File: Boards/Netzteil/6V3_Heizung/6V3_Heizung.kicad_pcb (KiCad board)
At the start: 2 copper layers, 100 x 80 mm, 65 parts, among them P1 7V5_AC, P2 12V_DC, P3 6V3_DC_1, P4 6V3_DC_2, P5 Relais, Q1 IRF540N, Q2 IRF540N, Q3 BS170, U1 TL072, U2 LM393

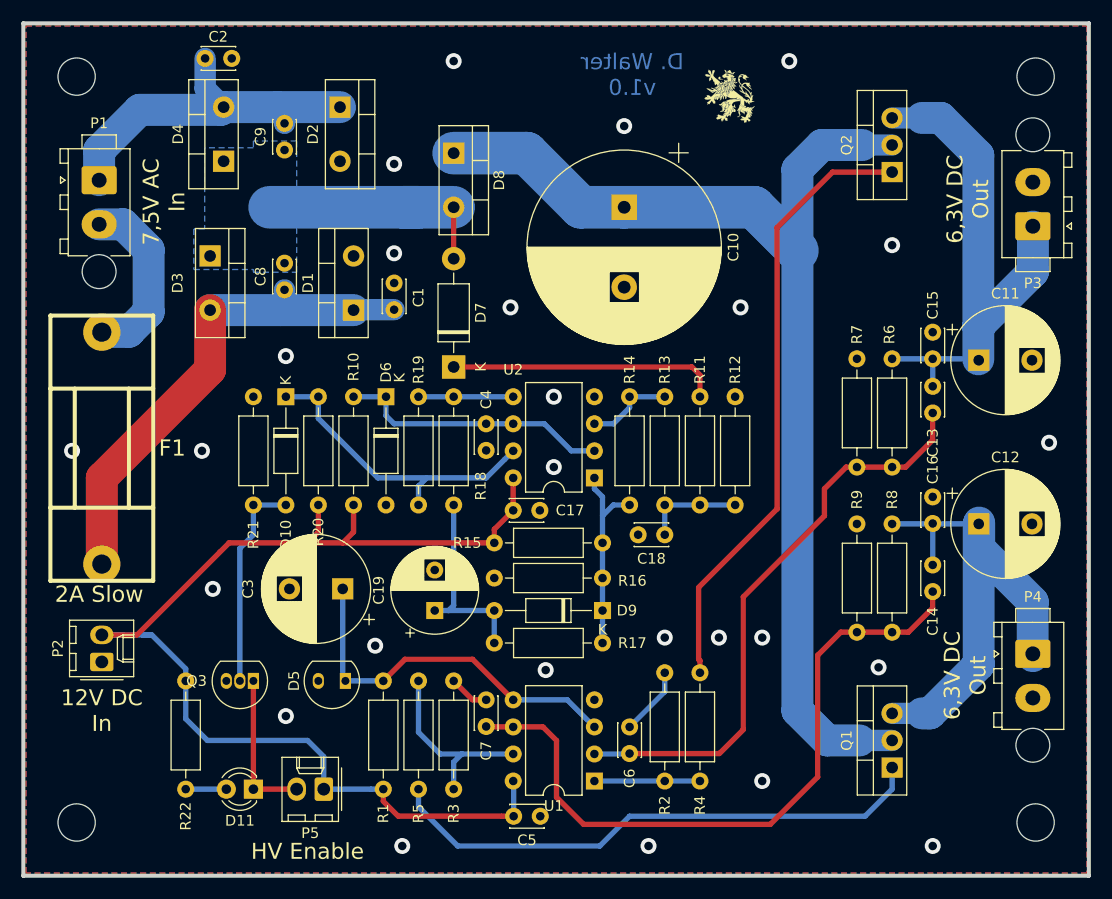
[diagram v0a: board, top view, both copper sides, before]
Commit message: Added Power LEDs
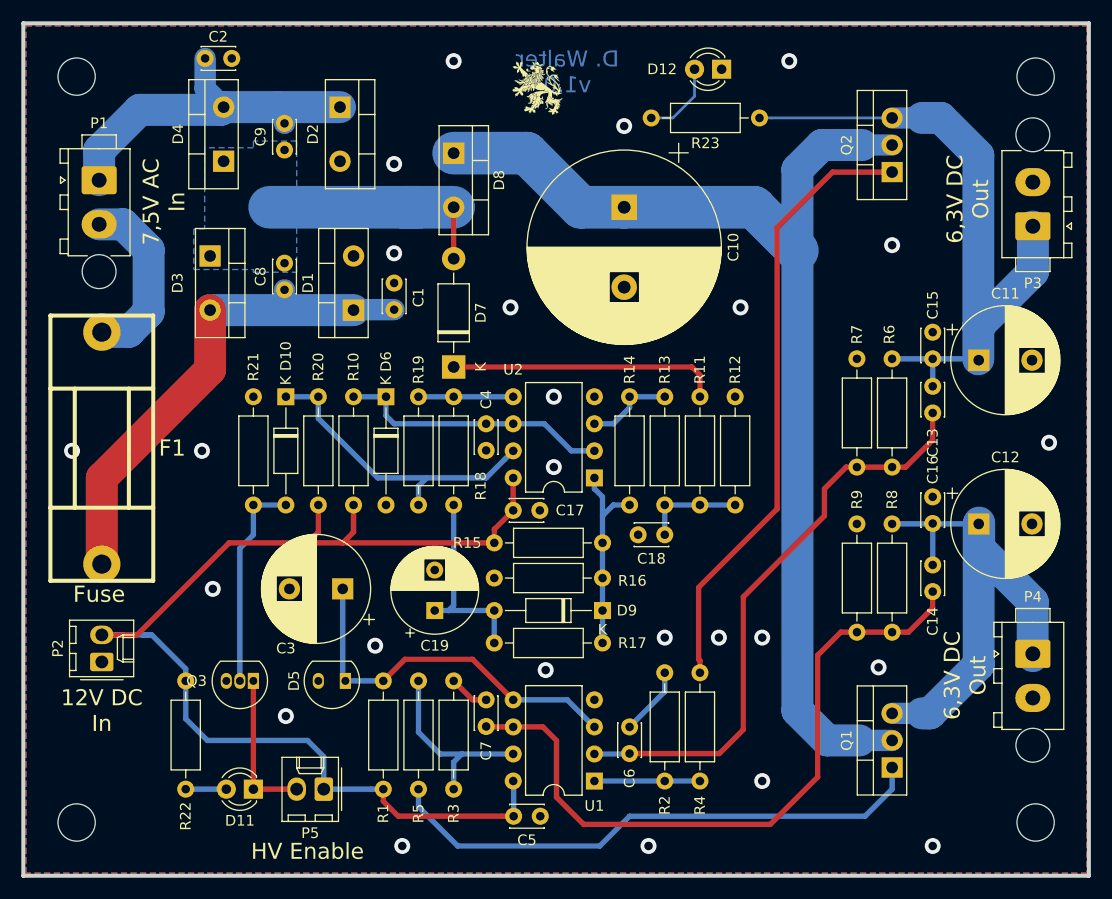
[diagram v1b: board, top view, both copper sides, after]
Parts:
- added D12: LED, LED_THT:LED_D3.0mm, F.Cu at (125.1, 43.2)
- added R23: 23k, Resistor_THT:R_Axial_DIN0207_L6.3mm_D2.5mm_P10.16mm_Horizontal, F.Cu at (128.7, 47.8)
- F1: value 2A Slow -> Fuse
- moved G*** 18.1 mm to (107.8, 45.0)
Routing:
- net Net-(C11-Pad1): track 52.8 -> 65.3 mm
- net Net-(D12-Pad2): track 0.00 -> 7.45 mm
- net GND: vias 26 -> 25

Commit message: Adjusted Silkscreen
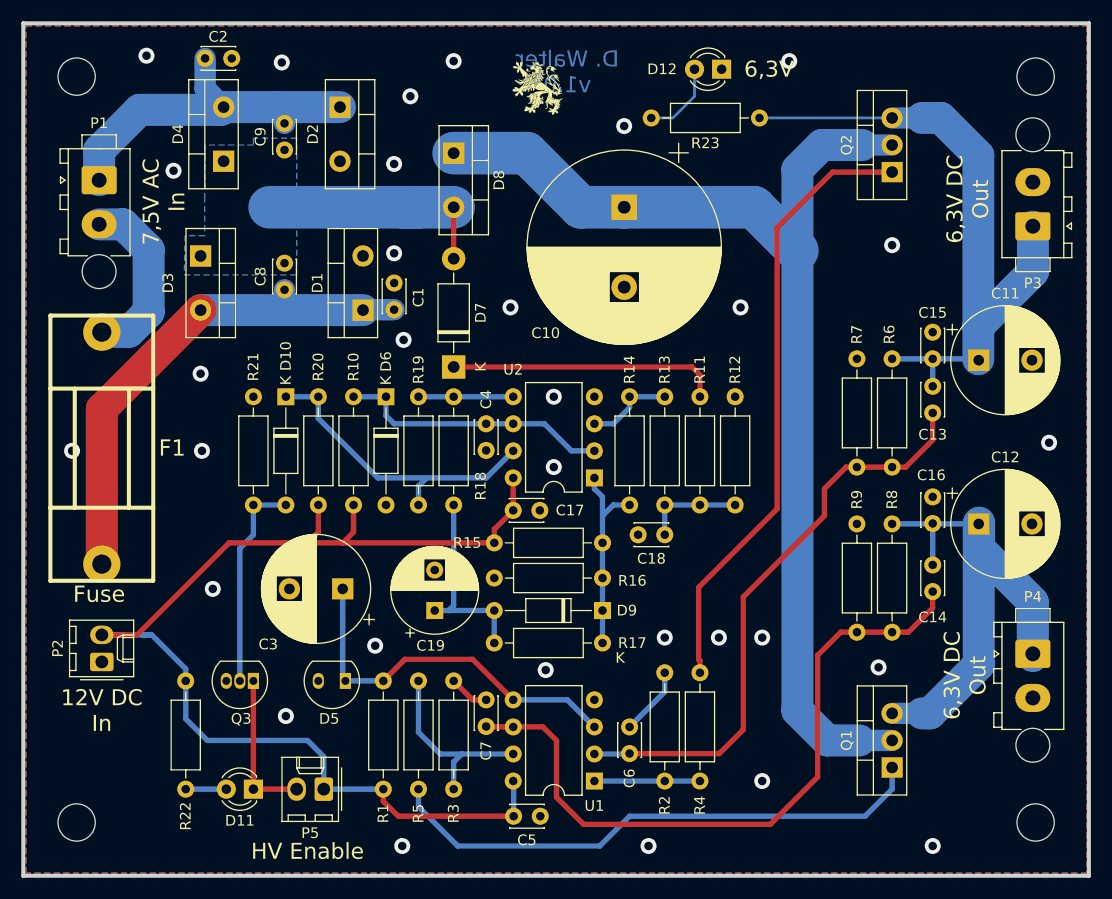
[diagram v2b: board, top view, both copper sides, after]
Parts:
- moved D1 0.89 mm to (91.4, 65.8)
- moved D3 0.89 mm to (76.2, 60.7)
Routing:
- net Net-(C1-Pad1): track 47.4 -> 48.8 mm
- net GND: vias 25 -> 31
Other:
- board text added: "6,3V"
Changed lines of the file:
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@@
   (general
     (thickness 1.6)
-    (drawings 6)
-    (tracks 240)
+    (drawings 7)
+    (tracks 244)
     (zones 0)
     (modules 67)
@@
     (47 F.CrtYd user)
     (48 B.Fab user)
-    (49 F.Fab user)
+    (49 F.Fab user hide)
   )
   (setup
-    (last_trace_width 0.25)
+    (last_trace_width 3)
     (user_trace_width 0.5)
     (user_trace_width 1)
@@
       (effects (font (size 1 1) (thickness 0.15)))
     )
-    (fp_text user K (at 0 -1.8) (layer F.SilkS)
+    (fp_text user K (at -1.651 -4.445) (layer F.SilkS)
       (effects (font (size 1 1) (thickness 0.15)))
     )
@@
     (descr "TO-92 leads in-line, narrow, oval pads, drill 0.75mm (see NXP sot054_po.pdf)")
     (tags "to-92 sc-43 sc-43a sot54 PA33 transistor")
-    (fp_text reference Q3 (at 5.334 0) (layer F.SilkS)
+    (fp_text reference Q3 (at 1.143 -3.556) (layer F.SilkS)
       (effects (font (size 1 1) (thickness 0.15)))
     )
@@
     (descr "CP, Radial series, Radial, pin pitch=3.80mm, , diameter=8mm, Electrolytic Capacitor")
     (tags "CP Radial series Radial pin pitch 3.80mm  diameter 8mm Electrolytic Capacitor")
-    (fp_text reference C19 (at -3.302 0 180) (layer F.SilkS)
+    (fp_text reference C19 (at -3.302 -0.381 180) (layer F.SilkS)
       (effects (font (size 1 1) (thickness 0.15)))
     )
@@
     (descr "CP, Radial series, Radial, pin pitch=7.50mm, , diameter=18mm, Electrolytic Capacitor")
     (tags "CP Radial series Radial pin pitch 7.50mm  diameter 18mm Electrolytic Capacitor")
-    (fp_text reference C10 (at 3.75 -10.25 270) (layer F.SilkS)
+    (fp_text reference C10 (at 11.811 7.366) (layer F.SilkS)
       (effects (font (size 1 1) (thickness 0.15)))
     )
@@
     (descr "TO-92 2-pin leads in-line, narrow, oval pads, drill 0.75mm (see NXP sot054_po.pdf)")
     (tags "to-92 sc-43 sc-43a sot54 PA33 diode SOD70")
-    (fp_text reference D5 (at 4.826 0 270) (layer F.SilkS)
+    (fp_text reference D5 (at 1.524 -3.556) (layer F.SilkS)
       (effects (font (size 1 1) (thickness 0.15)))
     )
@@
   )
   (module Package_TO_SOT_THT:TO-220-2_Vertical (layer F.Cu)
-    (at 77.089 60.706 270)
+    (at 76.2 60.706 270)
     (descr "TO-220-2, Vertical, RM 5.08mm, see https://www.centralsemi.com/PDFS/CASE/TO-220-2PD.PDF")
     (tags "TO-220-2 Vertical RM 5.08mm")
@@
   )
   (module Package_TO_SOT_THT:TO-220-2_Vertical (layer F.Cu)
-    (at 90.551 65.786 90)
+    (at 91.44 65.786 90)
     (descr "TO-220-2, Vertical, RM 5.08mm, see https://www.centralsemi.com/PDFS/CASE/TO-220-2PD.PDF")
     (tags "TO-220-2 Vertical RM 5.08mm")
@@
     (descr "C, Disc series, Radial, pin pitch=2.50mm, , diameter*width=3*2mm^2, Capacitor")
     (tags "C Disc series Radial pin pitch 2.50mm  diameter 3mm width 2mm Capacitor")
-    (fp_text reference C16 (at -2.54 0 270) (layer F.SilkS)
+    (fp_text reference C16 (at -2.032 0.127) (layer F.SilkS)
       (effects (font (size 1 1) (thickness 0.15)))
     )
@@
     (descr "C, Disc series, Radial, pin pitch=2.50mm, , diameter*width=3*2mm^2, Capacitor")
     (tags "C Disc series Radial pin pitch 2.50mm  diameter 3mm width 2mm Capacitor")
-    (fp_text reference C15 (at -2.54 0 270) (layer F.SilkS)
+    (fp_text reference C15 (at -1.818 0) (layer F.SilkS)
       (effects (font (size 1 1) (thickness 0.15)))
     )
@@
     (descr "C, Disc series, Radial, pin pitch=2.50mm, , diameter*width=3*2mm^2, Capacitor")
     (tags "C Disc series Radial pin pitch 2.50mm  diameter 3mm width 2mm Capacitor")
-    (fp_text reference C14 (at -2.794 0 90) (layer F.SilkS)
+    (fp_text reference C14 (at -2.413 0 180) (layer F.SilkS)
       (effects (font (size 1 1) (thickness 0.15)))
     )
@@
     (descr "C, Disc series, Radial, pin pitch=2.50mm, , diameter*width=3*2mm^2, Capacitor")
     (tags "C Disc series Radial pin pitch 2.50mm  diameter 3mm width 2mm Capacitor")
-    (fp_text reference C13 (at -2.794 0 90) (layer F.SilkS)
+    (fp_text reference C13 (at -2.032 0 180) (layer F.SilkS)
       (effects (font (size 1 1) (thickness 0.15)))
     )
@@
     (descr "CP, Radial series, Radial, pin pitch=5.00mm, , diameter=10mm, Electrolytic Capacitor")
     (tags "CP Radial series Radial pin pitch 5.00mm  diameter 10mm Electrolytic Capacitor")
-    (fp_text reference C3 (at 5.334 -5.588) (layer F.SilkS)
+    (fp_text reference C3 (at 6.985 -5.207) (layer F.SilkS)
       (effects (font (size 1 1) (thickness 0.15)))
     )
@@
     )
   )
+  (gr_text 6,3V (at 129.54 43.18) (layer F.SilkS)
+    (effects (font (size 1.5 1.5) (thickness 0.3)))
+  )
   (gr_text "6,3V DC\nOut" (at 147.955 100.076 90) (layer F.SilkS)
     (effects (font (size 1.5 1.5) (thickness 0.3)))
@@
   (segment (start 84.074 65.405) (end 83.693 65.786) (width 2) (layer B.Cu) (net 1))
   (segment (start 84.074 63.881) (end 84.074 65.405) (width 2) (layer B.Cu) (net 1))
-  (segment (start 77.089 65.786) (end 83.693 65.786) (width 3) (layer B.Cu) (net 1))
-  (segment (start 83.693 65.786) (end 90.551 65.786) (width 3) (layer B.Cu) (net 1))
-  (segment (start 77.089 71.374) (end 77.089 65.786) (width 3) (layer F.Cu) (net 1))
-  (segment (start 66.929 89.6239) (end 66.929 81.534) (width 3) (layer F.Cu) (net 1))
-  (segment (start 66.929 81.534) (end 77.089 71.374) (width 3) (layer F.Cu) (net 1))
+  (segment (start 66.929 75.057) (end 76.2 65.786) (width 3) (layer F.Cu) (net 1))
+  (segment (start 66.929 89.6239) (end 66.929 75.057) (width 3) (layer F.Cu) (net 1))
+  (segment (start 76.2 65.786) (end 91.44 65.786) (width 3) (layer B.Cu) (net 1))
   (via (at 119.761 96.52) (size 1.5) (drill 0.8) (layers F.Cu B.Cu) (net 2))
   (via (at 124.841 96.52) (size 1.5) (drill 0.8) (layers F.Cu B.Cu) (net 2))
@@
   (via (at 95.123 116.078) (size 1.5) (drill 0.8) (layers F.Cu B.Cu) (net 2))
   (via (at 77.343 91.948) (size 1.5) (drill 0.8) (layers F.Cu B.Cu) (net 2))
+  (via (at 71.12 41.91) (size 1.5) (drill 0.8) (layers F.Cu B.Cu) (net 2))
+  (via (at 83.82 42.545) (size 1.5) (drill 0.8) (layers F.Cu B.Cu) (net 2))
+  (via (at 76.2 71.755) (size 1.5) (drill 0.8) (layers F.Cu B.Cu) (net 2))
+  (via (at 73.66 52.705) (size 1.5) (drill 0.8) (layers F.Cu B.Cu) (net 2))
+  (via (at 95.25 68.58) (size 1.5) (drill 0.8) (layers F.Cu B.Cu) (net 2))
+  (via (at 95.885 45.72) (size 1.5) (drill 0.8) (layers F.Cu B.Cu) (net 2))
   (segment (start 76.621 44.998) (end 78.359 46.736) (width 2) (layer B.Cu) (net 3) (status 20))
   (segment (start 76.621 42.164) (end 76.621 44.998) (width 2) (layer B.Cu) (net 3) (status 10))
@@
     (polygon
       (pts
-        (xy 76.581 50.546) (xy 76.581 55.118) (xy 76.581 58.166) (xy 75.565 58.166) (xy 75.565 61.976)
-        (xy 81.153 61.976) (xy 81.153 62.23) (xy 85.217 62.23) (xy 85.217 49.911) (xy 81.153 49.911)
-        (xy 81.153 50.546)
+        (xy 76.581 50.292) (xy 76.581 55.118) (xy 76.581 58.801) (xy 74.7395 58.801) (xy 74.676 62.484)
+        (xy 85.217 62.484) (xy 85.217 49.657) (xy 81.153 49.657) (xy 81.153 50.292)
       )
     )

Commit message: Added Mounting holes, Moved -60V Divider to HV Board, eliminated +450V Connector and Feedback Connector on Amp Board
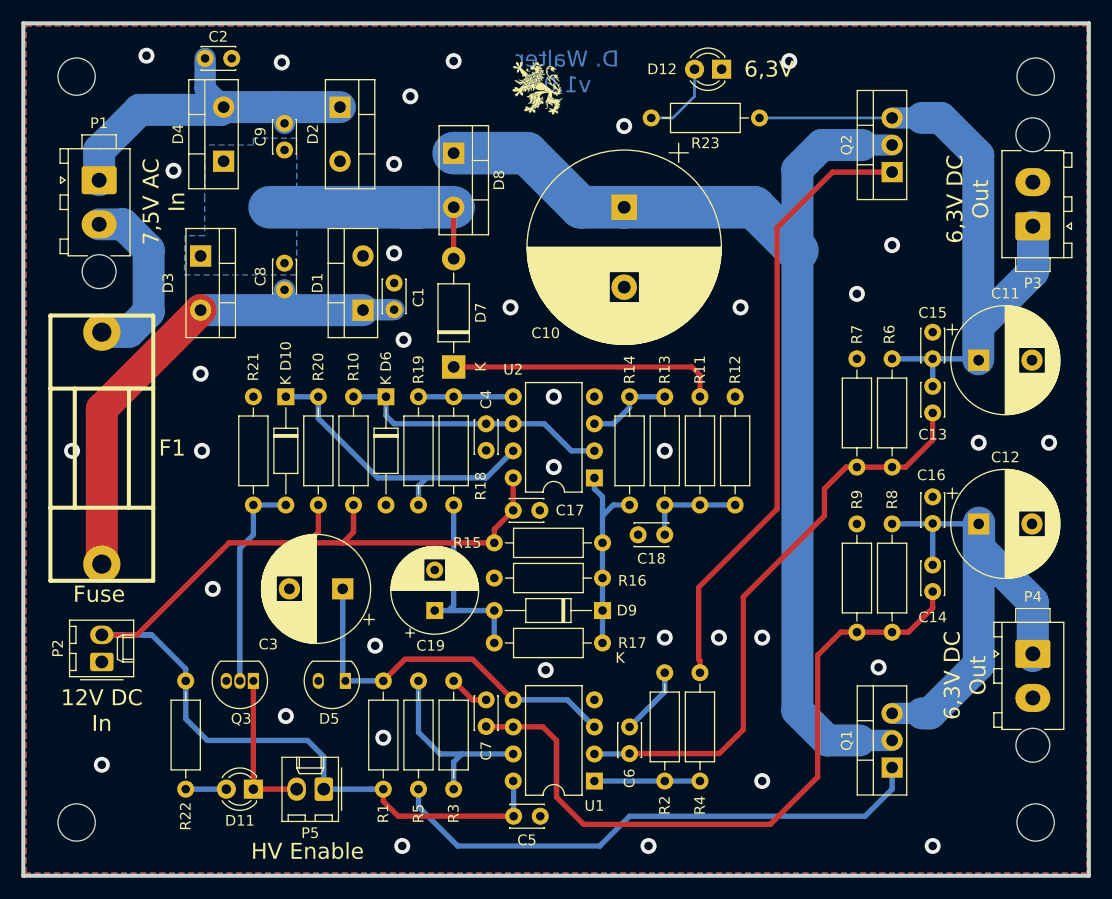
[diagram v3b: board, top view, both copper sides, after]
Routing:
- net GND: vias 31 -> 36
